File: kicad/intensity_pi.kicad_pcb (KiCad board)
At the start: 4 copper layers, 53.5 x 188.7 mm, 127 parts, among them J1 Input A, J2 Input B / Setpoint, J3 Monitor, J4 Output, J7 select 1, J8 Screw_Terminal_01x03, Q1 2N7002E, Q2 2N7002E, SW1 SW_SPDT, SW2 SW_SPDT, SW3 SW_SPDT, SW5 EG6100-ND, U1 LM4040DBZ-5, U10 OPA189, U11 PC817, U12 OPA189, U13 BUF634A, U14 TMUX6123, U17 TMUX6123, U18 OPA189, U19 L7815, U2 LM4040DBZ-5, U20 OPA189, U21 OPA189, U22 4x Comparator, U23 L7915, U3 INA849, U4 INA849, U5 OPA189, U7 OPA189, U8 BUF634A, U9 LM317_TO-252

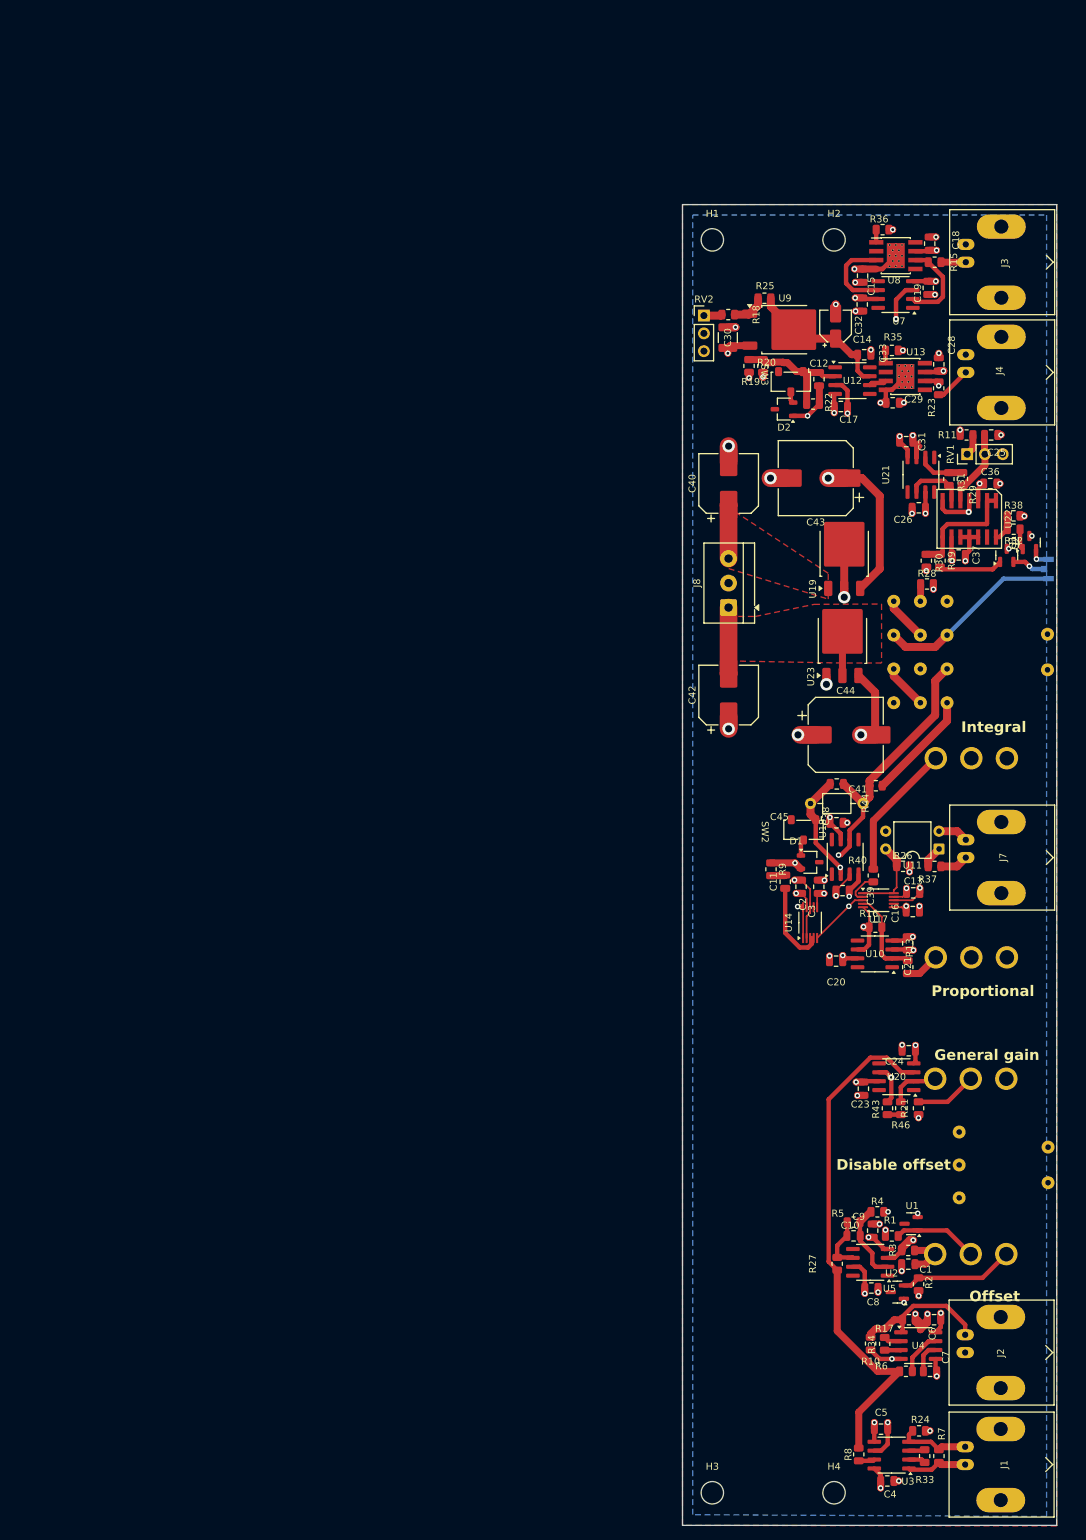
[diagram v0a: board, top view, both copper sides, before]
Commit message: Added 1k resistor to monitor, TODO: check BOM, reorg PI+LFGL, check power planes/return path, move A,B closer to PI, compress vertically
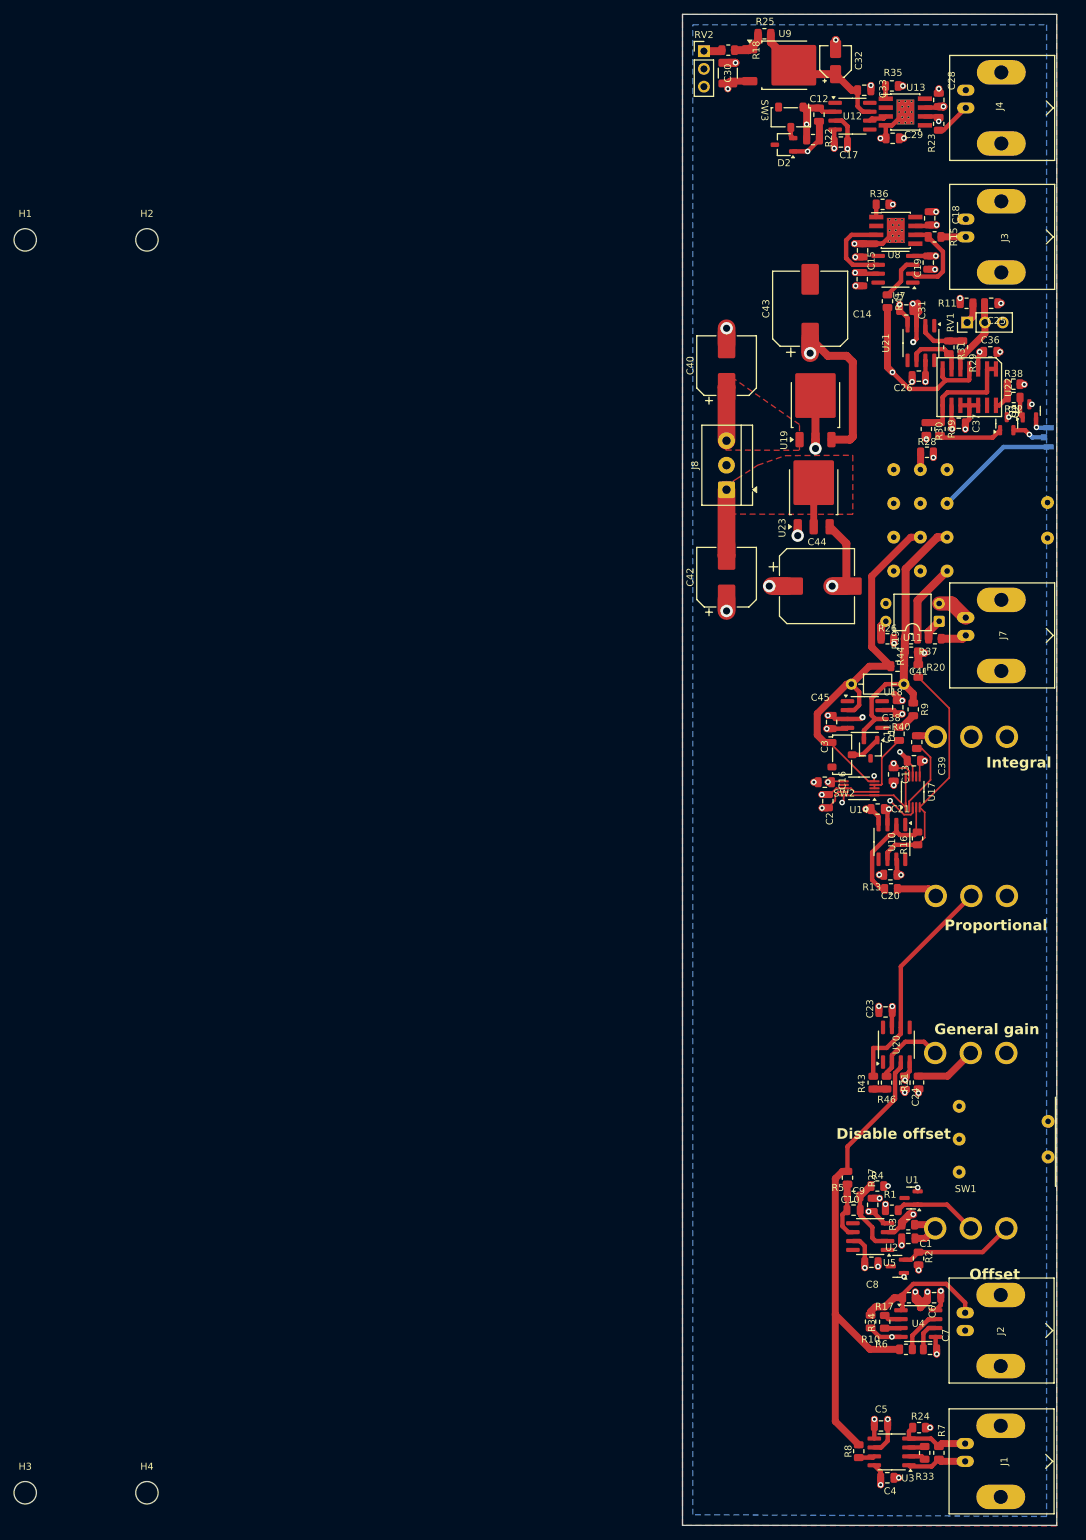
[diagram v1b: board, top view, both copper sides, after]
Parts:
- added R41: 1k, Resistor_SMD:R_0805_2012Metric, F.Cu at (234.3, -22.0)
- SW1: moved to F.Cu
- moved H2 98.2 mm to (128.5, -30.7)
- moved H4 98.2 mm to (128.5, 148.2)
- moved H1 98.2 mm to (111.1, -30.7)
- moved H3 98.2 mm to (111.1, 148.2)
- moved R20 49.8 mm to (238.7, 30.8)
- moved R19 46.1 mm to (237.7, 28.2), turned to 0 degrees
- moved C12 37.8 mm to (224.5, -48.6)
- moved C17 37.8 mm to (227.7, -44.7)
- moved C28 37.8 mm to (241.7, -50.7)
- moved C29 37.8 mm to (235.1, -45.2)
- moved C30 37.8 mm to (211.5, -54.6)
- moved C32 37.8 mm to (226.9, -56.2)
- moved C33 37.8 mm to (231.0, -52.1)
- moved R25 37.8 mm to (216.7, -60.2)
- moved RV2 37.8 mm to (208.1, -57.7)
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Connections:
- U7 pad 3: Error_signal -> Net-(U7-+)
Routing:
- net Net-(SW3-A): track 18.2 -> 98.2 mm, vias 0 -> 2
- net Net-(D1-A): track 106.4 -> 40.9 mm, vias 3 -> 0
- net Net-(R16-Pad2): track 95.7 -> 34.0 mm, vias 2 -> 0
- net Net-(R12-Pad2): track 19.5 -> 2.78 mm
- net Net-(U14C-SEL1): track 34.1 -> 46.4 mm
- net Net-(SW1-A): track 14.0 -> 23.1 mm
- net Net-(SW2-A): track 58.1 -> 66.4 mm
- net Net-(U7-+): track 0.00 -> 6.32 mm
- net Net-(R40-Pad2): track 4.74 -> 10.9 mm
- net Net-(U10--): track 12.9 -> 18.7 mm
- net Net-(R44-Pad1): track 15.7 -> 11.4 mm
- net Net-(U20--): track 7.01 -> 11.0 mm
- net Net-(C11-Pad1): track 12.6 -> 8.86 mm
- net Error_signal: track 142.7 -> 139.9 mm, vias 3 -> 1
- net Net-(U20-+): track 73.7 -> 71.6 mm
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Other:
- board size 53.5 x 188.7 mm -> 53.5 x 215.9 mm

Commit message: Updated Design, more compact layout, precise location values for I/O, Fixed TrimPot footprint, TODO: Finalize BOM, add partnos for SMD R/Cs
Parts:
- removed H3, H4: MountingHole, MountingHole:MountingHole_3.2mm_M3_ISO14580
- R12: moved to F.Cu
- RV1, RV2: footprint Connector_PinHeader_2.54mm:PinHeader_1x03_P2.54mm_Vertical -> Potentiometer_THT:Potentiometer_Bourns_3296W_Vertical
- moved C25 283.6 mm to (-31.4, -63.2), turned to -90 degrees
- moved R11 279.6 mm to (-31.4, -59.7), turned to -90 degrees
- moved C37 277.2 mm to (-27.8, -56.2), turned to -90 degrees
- moved D1 276.9 mm to (-33.2, -38.0), turned to 0 degrees
- moved RV1 276.8 mm to (-27.6, -63.0), turned to -90 degrees
- moved R20 275.6 mm to (-28.9, -34.7), turned to 180 degrees
- moved R19 272.4 mm to (-28.0, -32.1), turned to 90 degrees
- moved R9 271.9 mm to (-25.3, -31.4), turned to 0 degrees
- moved C38 271.3 mm to (-26.0, -34.9), turned to -90 degrees
- moved C36 271.0 mm to (-18.4, -58.9), turned to 90 degrees
- moved R31 270.1 mm to (-23.1, -61.1), turned to 0 degrees
- moved SW2 268.9 mm to (-28.0, -39.9), turned to -90 degrees
- moved C11 268.5 mm to (-23.4, -29.4), turned to 180 degrees
- moved C32 267.9 mm to (-39.2, -87.3), turned to 180 degrees
- moved R29 267.3 mm to (-18.2, -62.3)
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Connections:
- C25 pad 2: Net-(U22A-+) -> Net-(U22D-+)
- R29 pad 1: Net-(U22A-+) -> Net-(U22D-+)
- R30 pad 1: Net-(U22C--) -> Net-(U22B--)
- R31 pad 2: Net-(U22B--) -> Net-(U22C--)
- R39 pad 1: Net-(U22C--) -> Net-(U22B--)
- RV1 pad 2: Net-(U22A-+) -> Net-(U22D-+)
- U21 pad 6: Net-(U22B--) -> Net-(U22C--)
- U22 pad 1: Net-(U22C--) -> Net-(R32-Pad2)
- U22 pad 10: -15V -> Error_signal
- U22 pad 11: -15V -> Net-(U22D-+)
- U22 pad 13: unconnected-(U22-Pad13) -> Net-(U22B--)
- U22 pad 14: Net-(R32-Pad2) -> Net-(U22B--)
- U22 pad 2: Net-(U22C--) -> unconnected-(U22-Pad2)
- U22 pad 4: Error_signal -> GND
- U22 pad 5: Net-(U22A-+) -> GND
- U22 pad 7: Error_signal -> GND
- U22 pad 9: GND -> Error_signal
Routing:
- net Net-(U14C-SEL1): track 46.4 -> 116.9 mm, vias 1 -> 0
- net Error_signal: track 139.9 -> 91.2 mm, vias 1 -> 3
- net Net-(U22D-+): track 0.00 -> 25.6 mm, vias 0 -> 2
- net Net-(SW3-A): track 98.2 -> 73.2 mm
- net Net-(SW2-A): track 66.4 -> 46.9 mm, vias 2 -> 0
- net Vlim+: track 19.0 -> 38.1 mm
- net Net-(D1-A): track 40.9 -> 58.4 mm, vias 0 -> 2
- net Net-(D3-K1): track 3.20 -> 19.0 mm
- net Net-(D3-K2): track 4.80 -> 16.2 mm
- net Net-(U22A-+): track 11.0 -> 0.00 mm
- net GND: track 93.1 -> 102.1 mm, vias 46 -> 47
- net Net-(U22B--): track 8.47 -> 16.3 mm
- net Net-(U22C--): track 16.9 -> 9.70 mm
- net Net-(Q2-G): track 9.16 -> 1.99 mm
- net Net-(R16-Pad2): track 34.0 -> 28.5 mm, vias 0 -> 3
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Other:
- board size 53.5 x 215.9 mm -> 62.8 x 172 mm

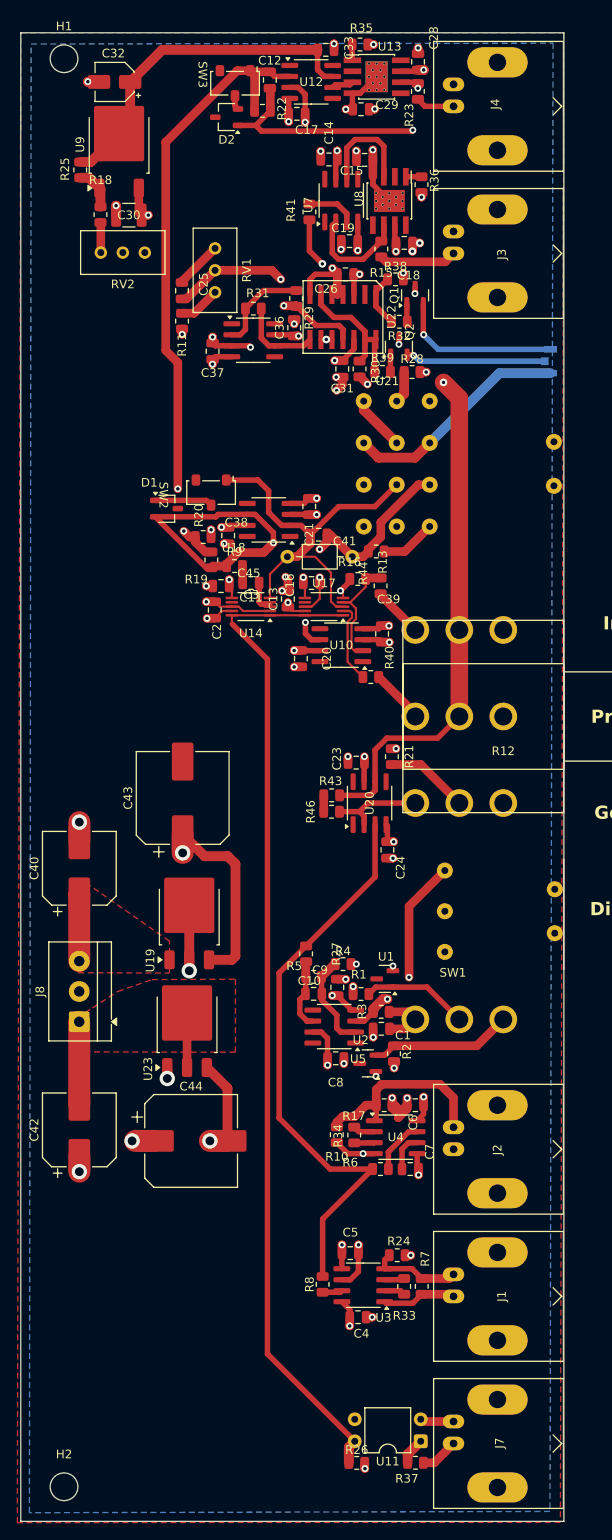
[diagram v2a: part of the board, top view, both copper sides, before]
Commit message: Minor Layout updates, replaced old component part no's, added part no's for rest of parts
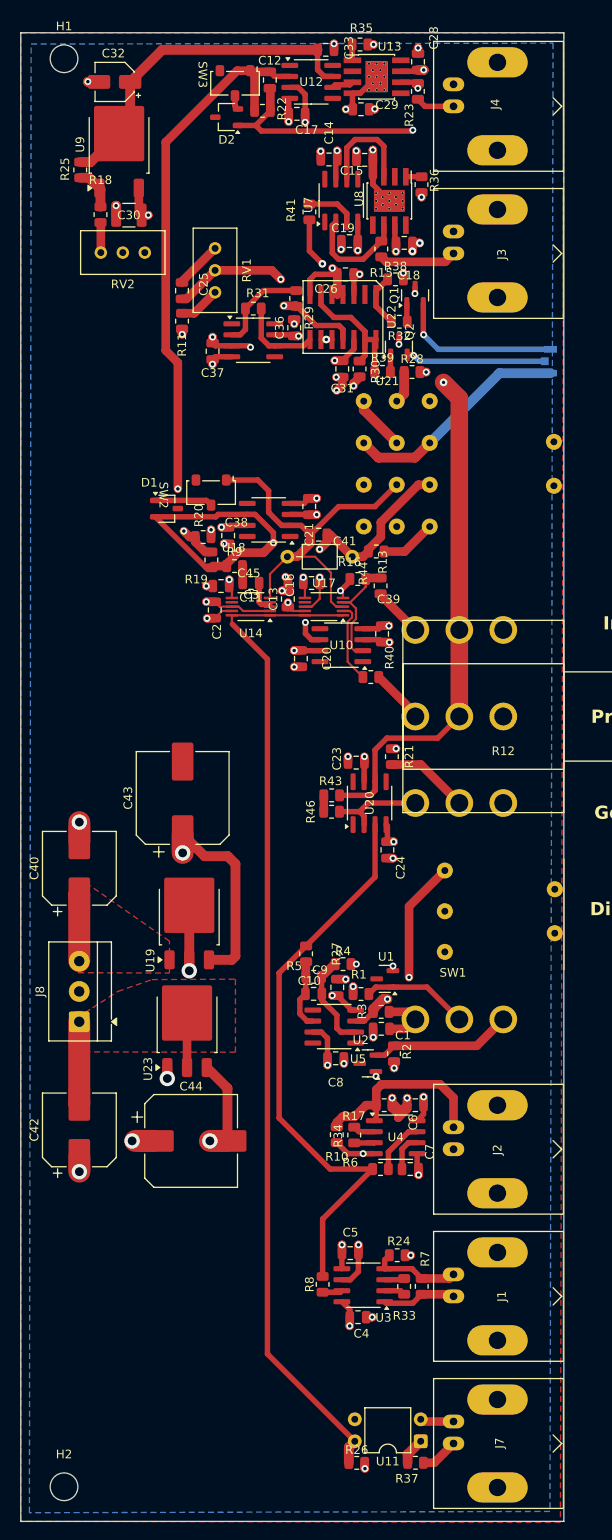
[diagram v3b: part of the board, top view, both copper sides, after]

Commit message: Minor Updates to layout, TODO: Redo PI layout
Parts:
- D3: moved to F.Cu
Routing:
- net Net-(D1-A): track 58.4 -> 49.5 mm
- net GND: track 102.1 -> 97.4 mm
- net Net-(D3-A): track 26.3 -> 29.3 mm, vias 0 -> 2
- net Net-(D3-K1): track 19.0 -> 21.0 mm, vias 1 -> 2
- net Net-(D3-K2): vias 1 -> 0
- net Error_signal: vias 3 -> 2

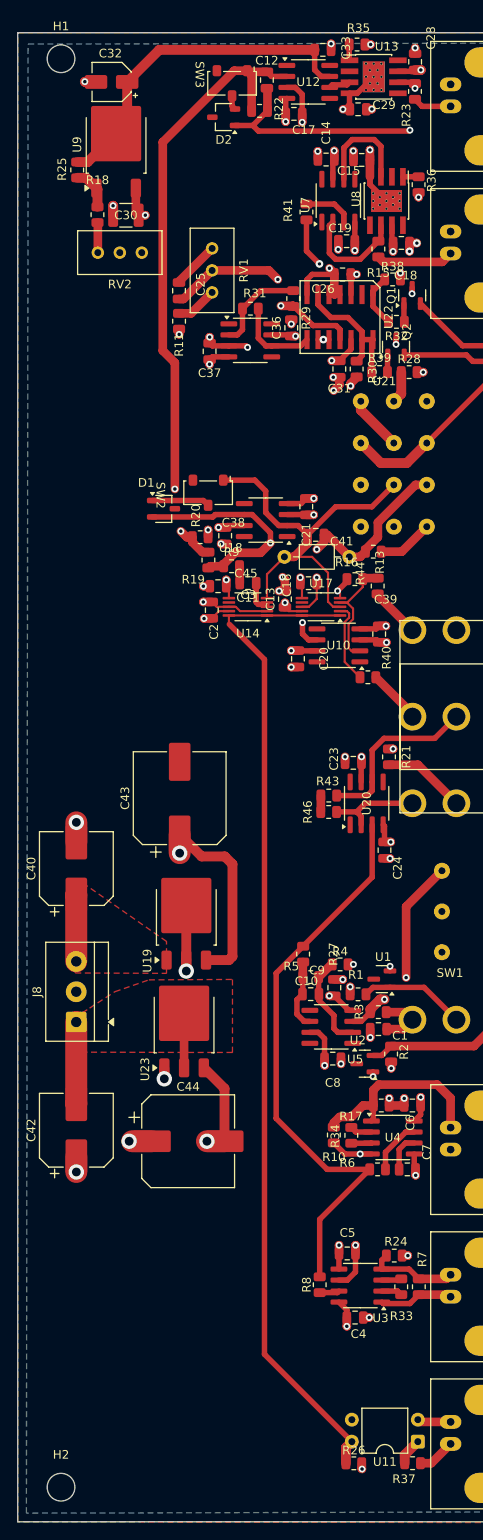
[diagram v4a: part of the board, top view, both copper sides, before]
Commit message: Reworked PI control layout, minimize feedback loop size
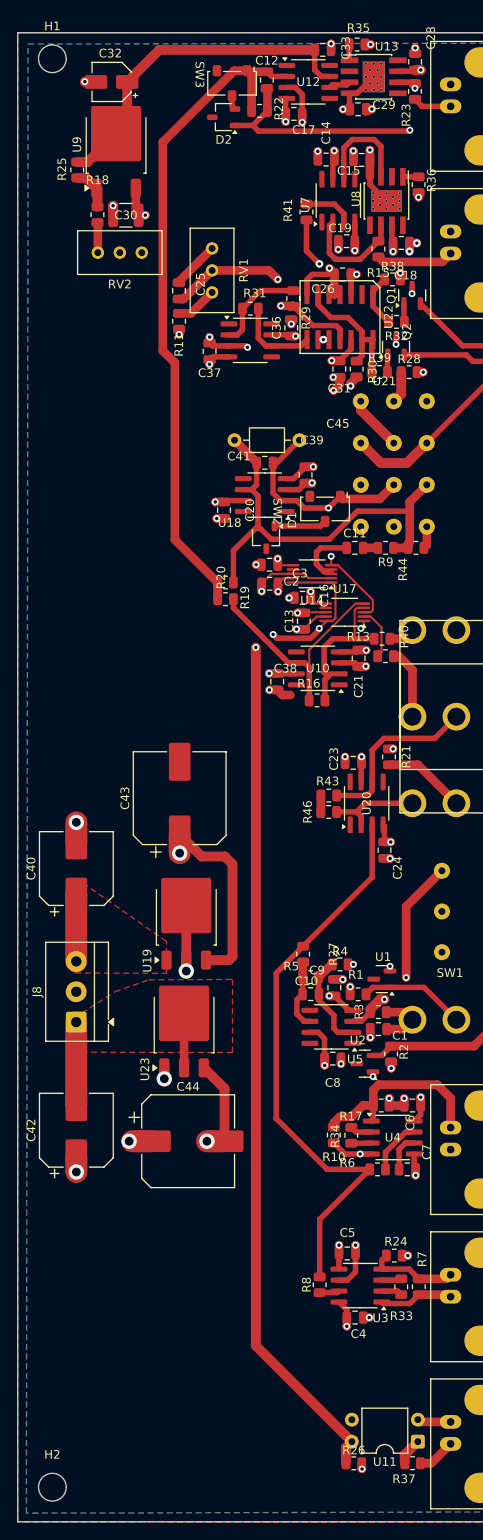
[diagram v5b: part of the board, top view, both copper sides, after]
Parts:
- moved C39 20.3 mm to (-16.7, -41.9)
- moved C20 19.2 mm to (-26.2, -37.9)
- moved C21 18.5 mm to (-10.6, -20.7)
- moved R9 17.9 mm to (-7.50, -33.5), turned to 180 degrees
- moved C38 17.9 mm to (-20.0, -18.0)
- moved R16 14.7 mm to (-15.4, -15.9)
- moved SW2 13.6 mm to (-14.5, -38.0)
- moved C45 13.6 mm to (-17.5, -45.9), turned to 180 degrees
- moved C11 13.0 mm to (-11.1, -33.5), turned to 0 degrees
- moved D1 12.3 mm to (-21.3, -34.7), turned to -90 degrees
- moved C41 10.2 mm to (-21.5, -43.3), turned to 0 degrees
- moved U14 8.33 mm to (-16.0, -30.5)
- moved R20 7.73 mm to (-26.0, -27.6)
- moved C2 7.35 mm to (-20.9, -29.4), turned to 180 degrees
- moved C3 6.45 mm to (-20.9, -31.6)
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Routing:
- net Net-(U14C-SEL1): track 116.9 -> 124.9 mm, vias 0 -> 4
- net Net-(SW2-A): track 46.9 -> 39.2 mm, vias 0 -> 2
- net Net-(U10--): track 13.4 -> 20.8 mm
- net Net-(SW3-A): track 73.2 -> 78.3 mm, vias 2 -> 0
- net Net-(R44-Pad1): track 6.47 -> 2.59 mm
- net Net-(C11-Pad1): track 4.06 -> 7.63 mm
- net Net-(R40-Pad2): track 9.48 -> 6.07 mm
- net Net-(R13-Pad1): track 5.84 -> 3.00 mm
- net Net-(R12-Pad2): track 5.99 -> 8.26 mm
- net -15V: track 60.9 -> 62.5 mm
- net Net-(R16-Pad2): track 28.5 -> 27.0 mm, vias 3 -> 0
- net +15V: track 72.8 -> 74.3 mm
- net GND: track 97.4 -> 98.7 mm, vias 47 -> 46
- net Net-(D1-K): track 6.69 -> 6.07 mm
- net Net-(D1-A): vias 2 -> 0
